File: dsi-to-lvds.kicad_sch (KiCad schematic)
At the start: 20 parts, among them Q8 PJE138K, U2 NTS0104_DHVQFN, U3 SN65DSI84

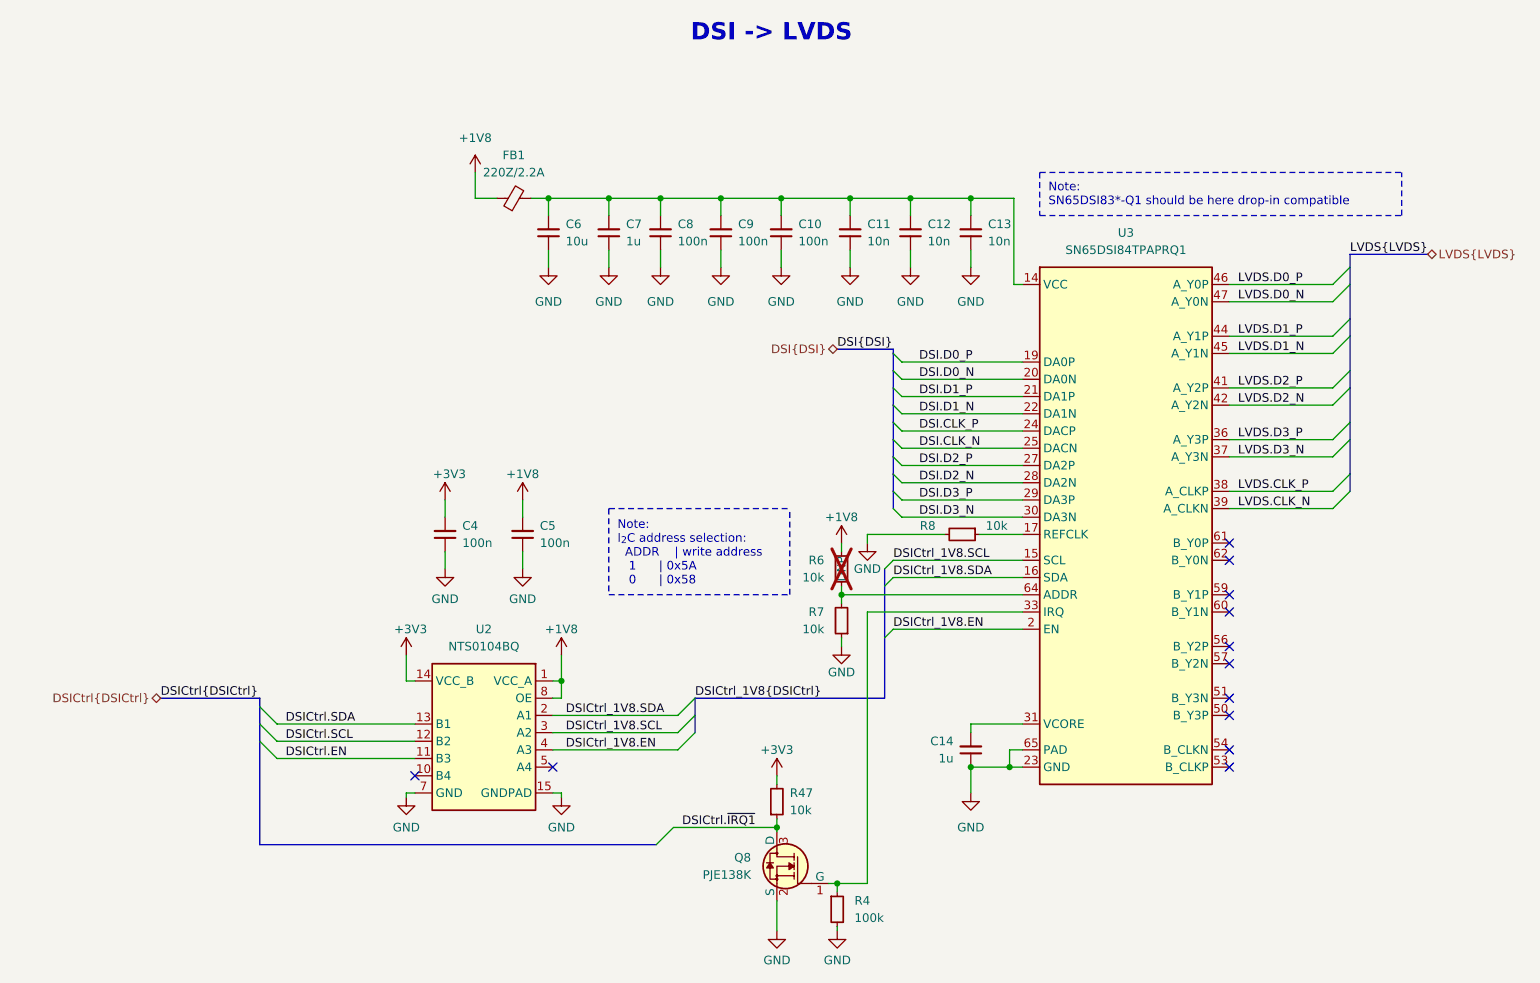
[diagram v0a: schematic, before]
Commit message: [#58170] Clean ERC (update from lib; align to grid)
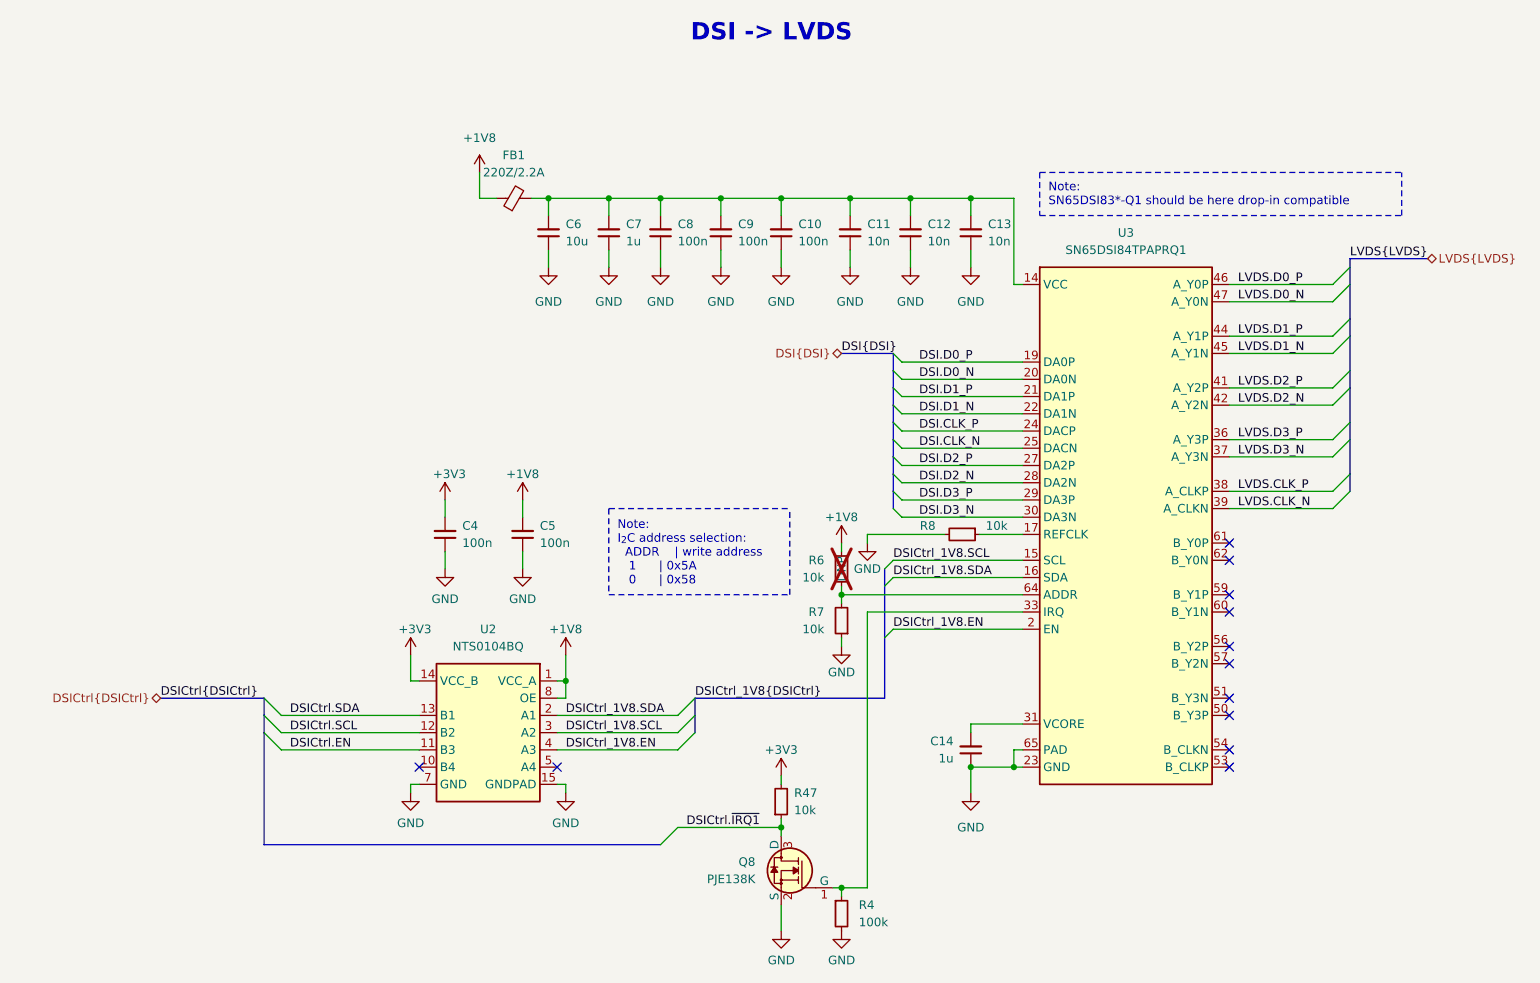
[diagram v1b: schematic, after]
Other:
- moved on the sheet: Q8, R4, R47, U2

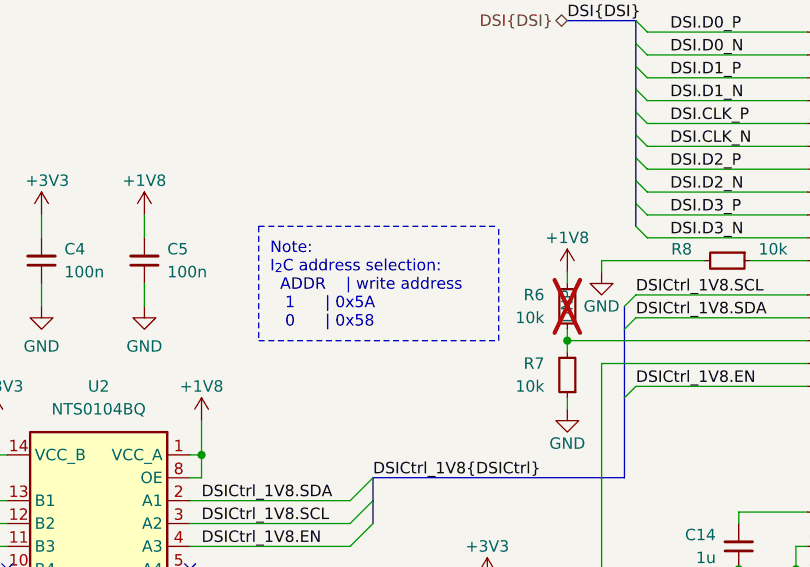
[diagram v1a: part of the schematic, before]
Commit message: [#58170] Sch: Change 8-bit I2C address to 7-bit
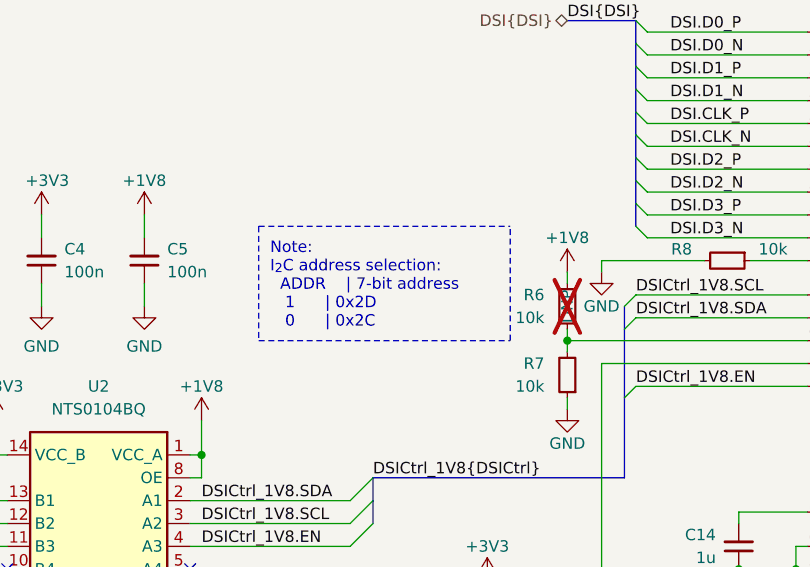
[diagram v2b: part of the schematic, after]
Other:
- note added: "Note: I_{2}C address selection: ADDR | 7-bit address 1 | 0x2D 0 | 0x2C"
- note removed: "Note: I_{2}C address selection: ADDR | write address 1 | 0x5A 0 | 0x58"
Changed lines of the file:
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@@
     (stroke (width 0) (type default))
   )
-  (polyline (pts (xy 132.08 110.49) (xy 158.75 110.49))
+  (polyline (pts (xy 132.08 110.49) (xy 160.02 110.49))
     (stroke (width 0) (type dash))
   )
@@
     (stroke (width 0) (type default))
   )
-  (polyline (pts (xy 132.08 97.79) (xy 158.75 97.79))
+  (polyline (pts (xy 132.08 97.79) (xy 160.02 97.79))
     (stroke (width 0) (type dash))
   )
@@
     (stroke (width 0) (type default))
   )
-  (polyline (pts (xy 158.75 110.49) (xy 158.75 97.79))
+  (polyline (pts (xy 160.02 110.49) (xy 160.02 97.79))
     (stroke (width 0) (type dash))
   )
@@
     (stroke (width 0) (type default))
   )
-  (text "Note:\nI_{2}C address selection:\n  ADDR	| write address\n   1  	| 0x5A\n   0  	| 0x58"
+  (text "Note:\nI_{2}C address selection:\n  ADDR	| 7-bit address\n   1  	| 0x2D\n   0  	| 0x2C"
     (at 133.35 109.22 0)
     (effects (font (size 1.27 1.27)) (justify left bottom))

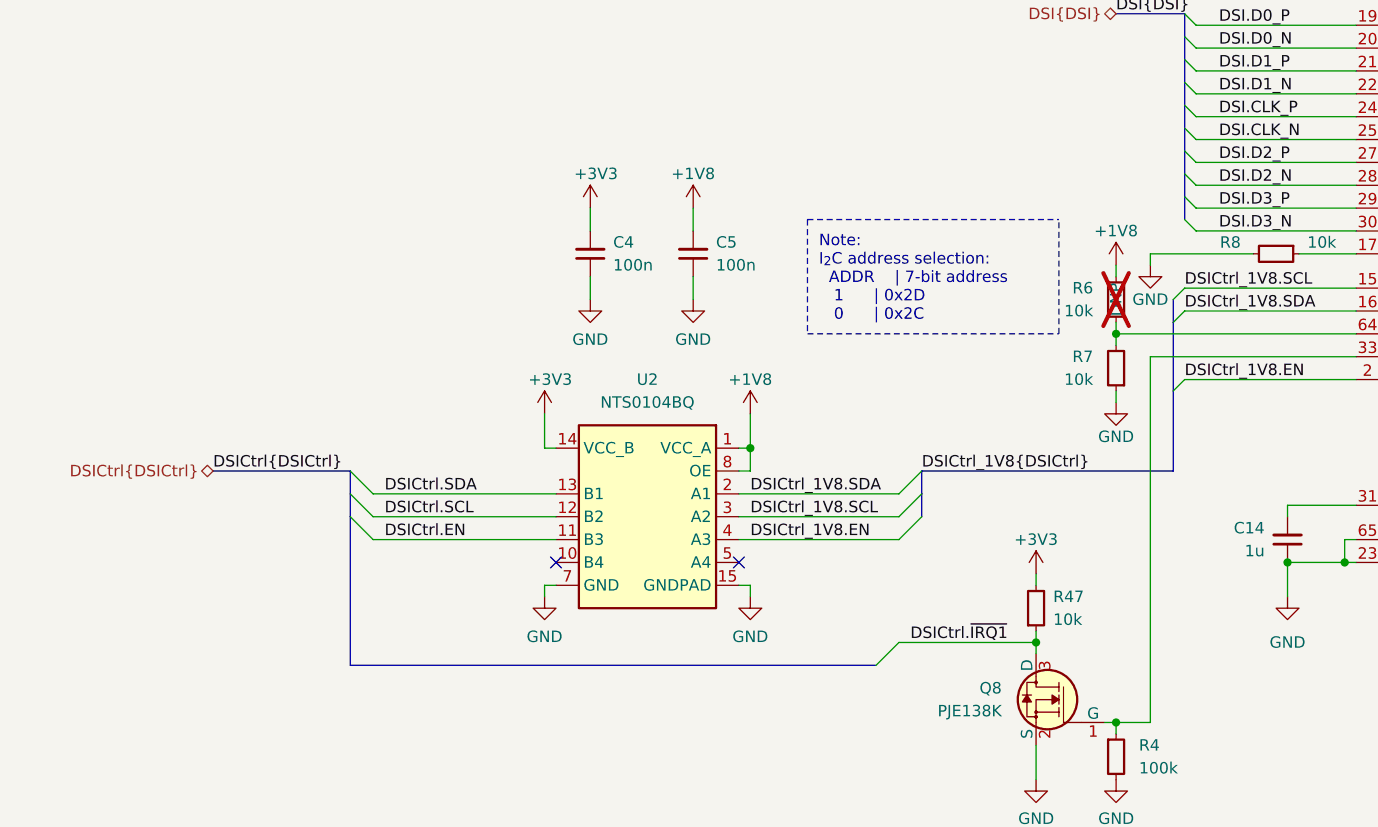
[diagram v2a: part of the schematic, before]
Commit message: [#58170] Add DNP pullups on I2C; Clean DRC
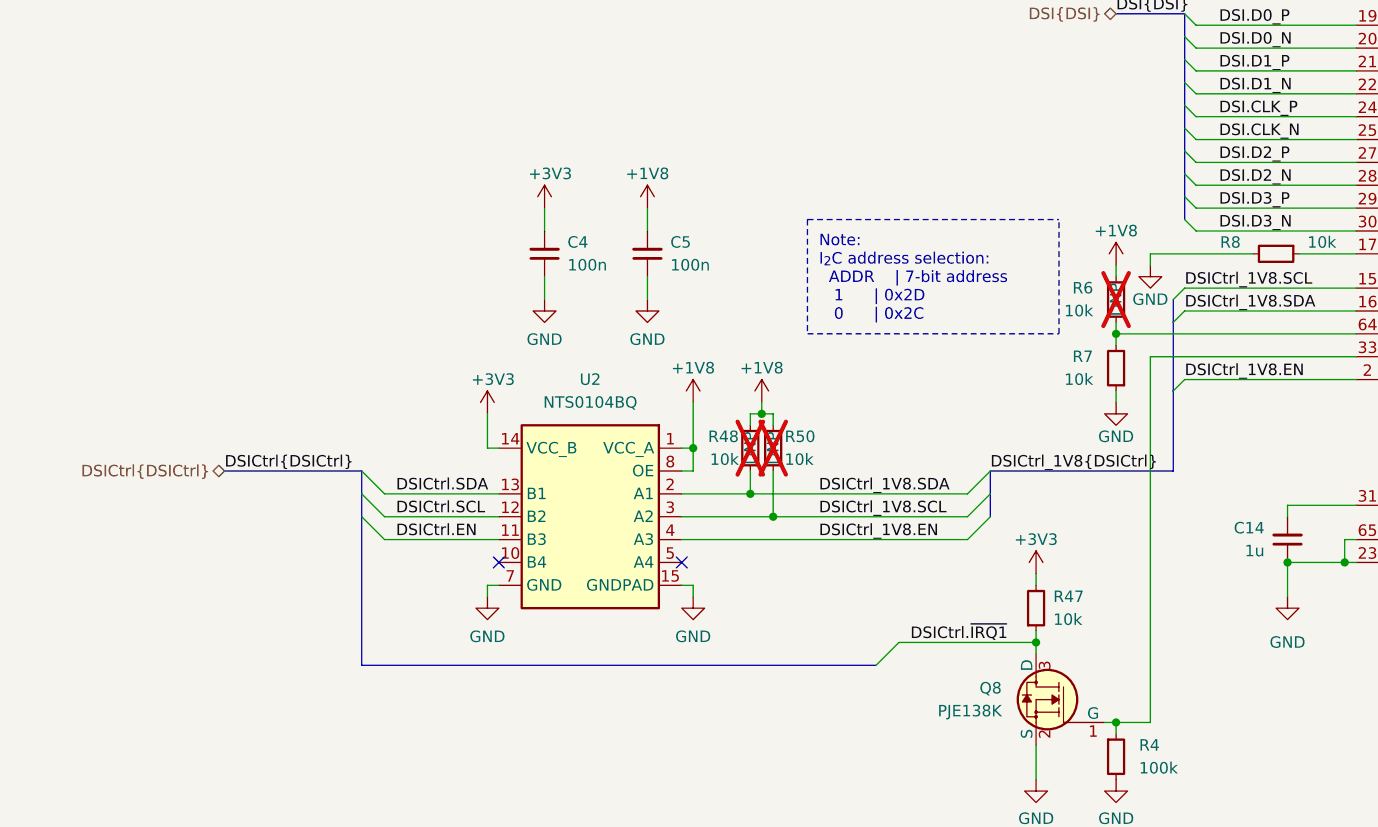
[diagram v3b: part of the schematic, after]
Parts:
- added R48, R50: R_10k_0402, antmicro-footprints:R_0402_1005Metric, symbol antmicroResistors0402:R_10k_0402
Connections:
- net +1V8: now also R48.2, R50.2
- net DSICtrl_1V8.SCL: now also R50.1
- net DSICtrl_1V8.SDA: now also R48.1
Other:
- moved on the sheet: C4, C5, U2
